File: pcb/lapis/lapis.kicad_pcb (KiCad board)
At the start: 2 copper layers, 42 x 58.6 mm, 80 parts, among them IC1 AS5047P-ATSM, IC2 AS5047P-ATSM, IC3 DRV8835DSSR, IC4 MIC5219-3.3YM5-TR, J1 Conn_01x03, J10 Conn_01x04, J11 Conn_01x01, J12 Conn_01x01, J13 Conn_01x01, J14 Conn_01x01, J2 Conn_01x03, J3 Conn_01x02, J4 Conn_01x03, J5 Conn_01x03, J6 Conn_01x03, J7 Conn_01x03, J8 Conn_01x03, J9 Conn_01x03, Q1 LTR-4206E, Q2 LTR-4206E, Q3 LTR-4206E, Q4 LTR-4206E, Q5 IRLML6402TRPBF, Q6 MMBF0201NLT1G, U1 STM32F411CEUx, U2 ICM-20602, U3 NJU6080, U4 NJU6080

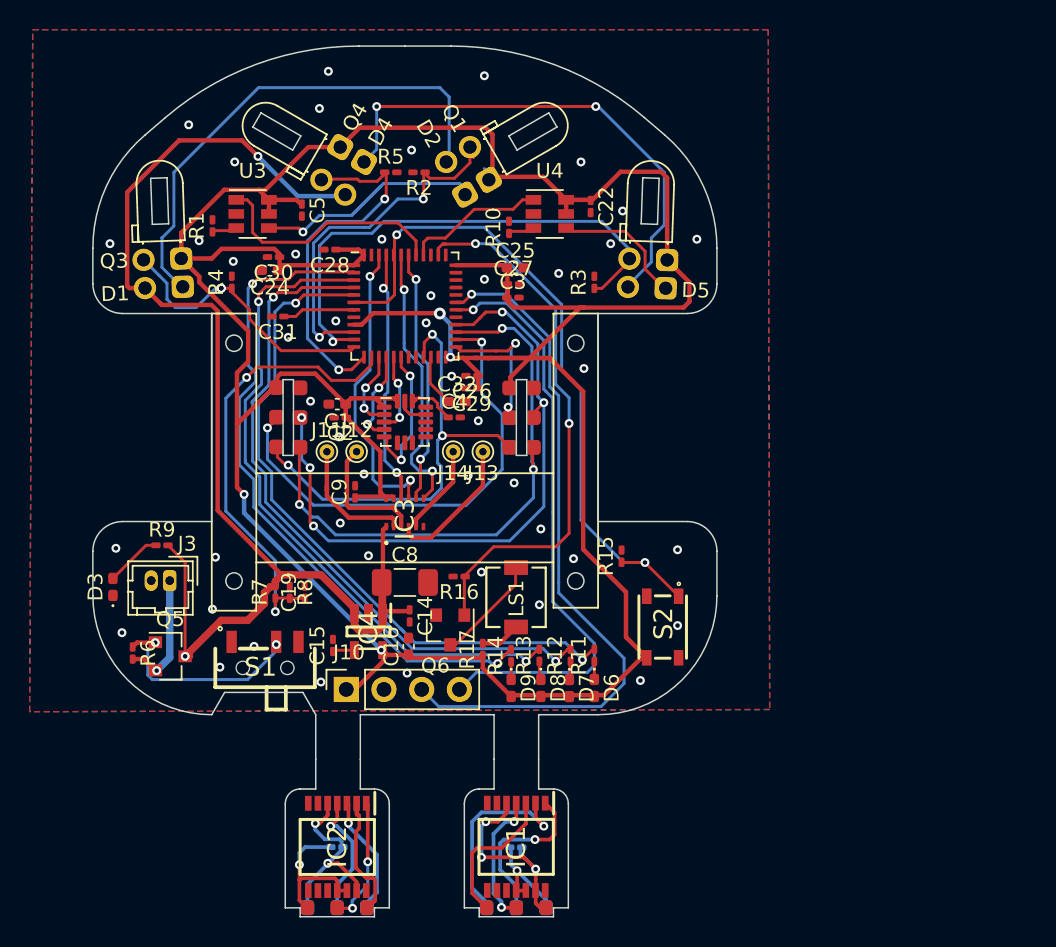
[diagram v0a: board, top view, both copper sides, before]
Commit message: STM411失敗基板　STM484に変更し基板修正
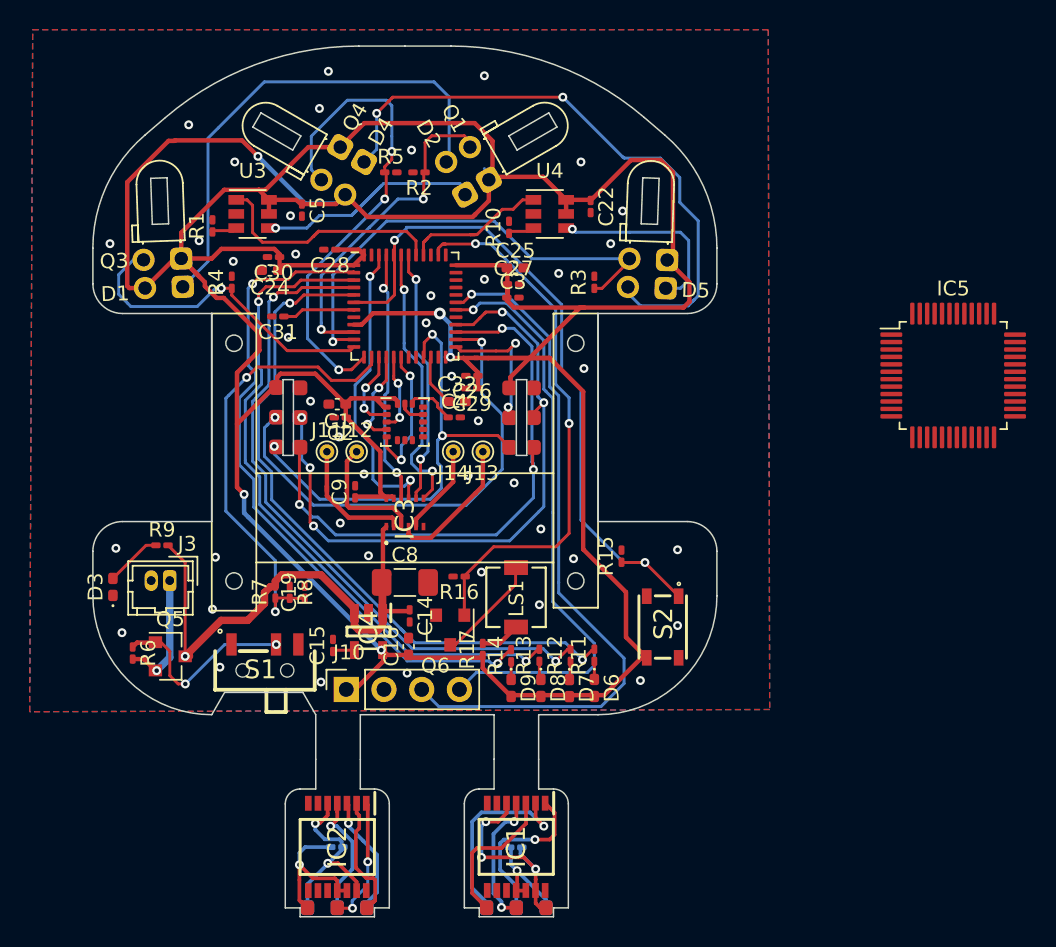
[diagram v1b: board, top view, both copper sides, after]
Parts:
- added IC5: STM32G484CET6, Package_QFP:LQFP-48_7x7mm_P0.5mm, F.Cu at (182.2, 100.9)
- moved S1 0.17 mm to (136.6, 119.0)
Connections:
- D1 pad 2: +BATT -> +3V3
- D4 pad 2: +BATT -> +3V3
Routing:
- net +BATT: track 89.4 -> 39.1 mm, vias 2 -> 1
- net +3V3: track 231.2 -> 279.9 mm, vias 4 -> 5
- net /WALL_SENSOR_LS/WALLSENSOR_ADC: track 25.2 -> 33.6 mm, vias 2 -> 3
- net Net-(D4-Pad1): track 34.0 -> 41.1 mm
- net Net-(D5-Pad1): track 8.41 -> 12.6 mm, vias 0 -> 1
- net /WALL_SENSOR_LF/WALLSENSOR_ADC: track 19.2 -> 22.5 mm, vias 2 -> 1
- net /WALL_SENSOR_RF/WALLSENSOR_ADC: track 34.6 -> 32.4 mm
- net /WALL_SENSOR_RS/WALLSENSOR_ADC: track 25.1 -> 24.0 mm
- net Net-(Q5-Pad1): track 14.0 -> 13.2 mm
- net Net-(D1-Pad1): track 33.9 -> 33.1 mm
- net Net-(C4-Pad1): track 3.78 -> 3.14 mm
- net /CPU/LED_LSRF: track 10.3 -> 10.9 mm
- net GND: vias 46 -> 43

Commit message: no message
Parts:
- removed IC5: STM32G484CET6, Package_QFP:LQFP-48_7x7mm_P0.5mm

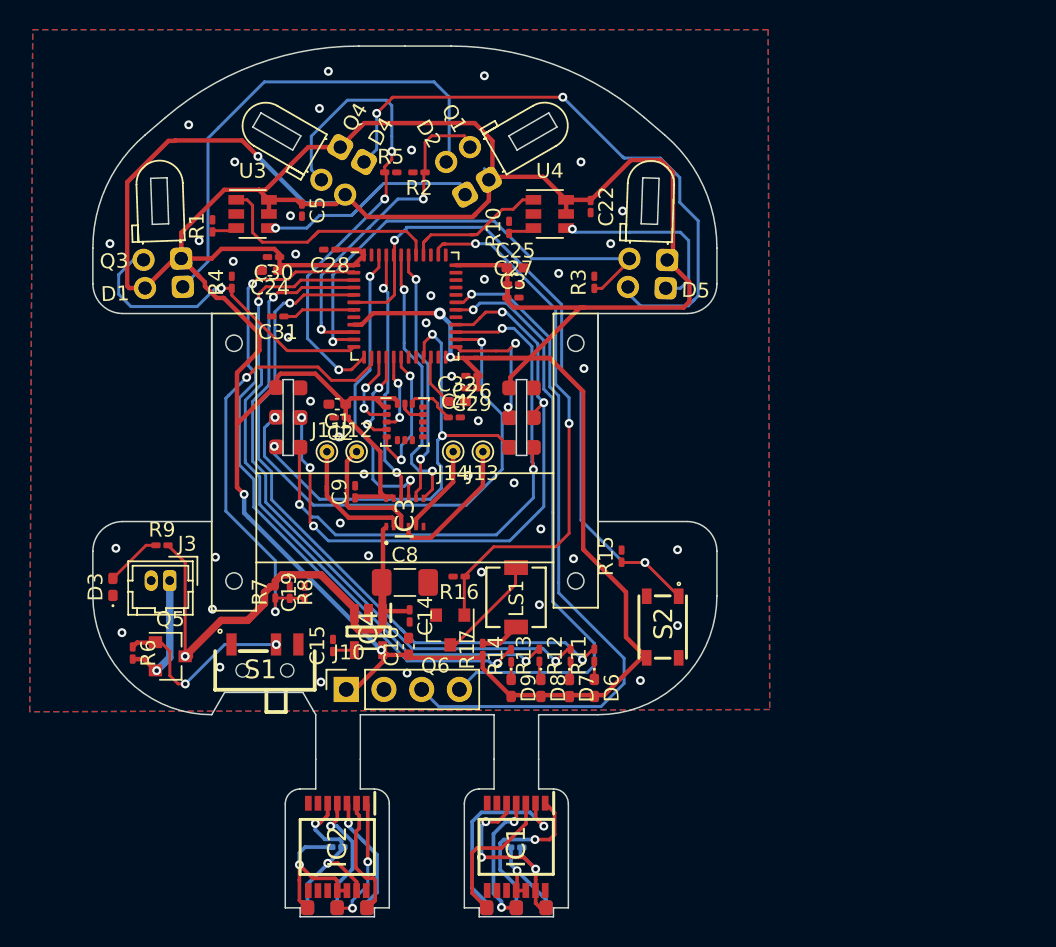
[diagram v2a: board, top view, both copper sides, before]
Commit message: 信地旋回探索
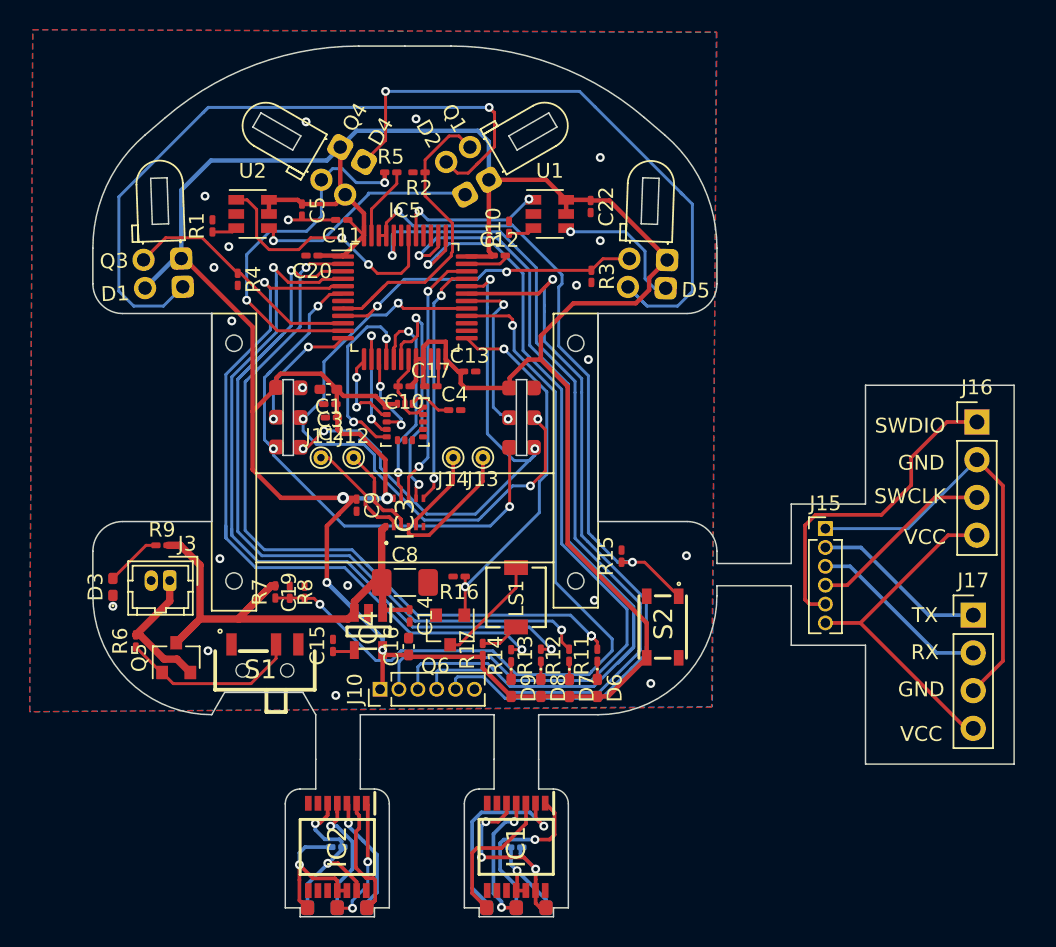
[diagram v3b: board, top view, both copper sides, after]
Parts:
- removed C24, C25, C32: 10u, Capacitor_SMD:C_0402_1005Metric_Pad0.74x0.62mm_HandSolder
- removed C26, C27, C28, C29, C30, C31: 0.1u, Capacitor_SMD:C_0201_0603Metric_Pad0.64x0.40mm_HandSolder
- removed the U1 at (145.2, 96.2)
- added C10: 0.1u, Capacitor_SMD:C_0201_0603Metric_Pad0.64x0.40mm_HandSolder, F.Cu at (145.2, 101.6)
- added C11: 0.1u, Capacitor_SMD:C_0201_0603Metric_Pad0.64x0.40mm_HandSolder, F.Cu at (141.0, 90.4)
- added C12: 0.1u, Capacitor_SMD:C_0201_0603Metric_Pad0.64x0.40mm_HandSolder, F.Cu at (151.6, 92.8)
- added C13: 0.1u, Capacitor_SMD:C_0201_0603Metric_Pad0.64x0.40mm_HandSolder, F.Cu at (149.6, 100.6)
- added C17: 1u, Capacitor_SMD:C_0201_0603Metric_Pad0.64x0.40mm_HandSolder, F.Cu at (147.0, 101.6)
- added C20: 1u, Capacitor_SMD:C_0201_0603Metric_Pad0.64x0.40mm_HandSolder, F.Cu at (139.0, 92.8)
- added IC5: STM32G484CET6, Package_QFP:LQFP-48_7x7mm_P0.5mm, F.Cu at (145.2, 95.6)
- added J15: Conn_01x06_Male, Connector_PinHeader_1.27mm:PinHeader_1x06_P1.27mm_Vertical, F.Cu at (173.6, 111.2)
- added J16: Conn_01x04_Female, Connector_PinHeader_2.54mm:PinHeader_1x04_P2.54mm_Vertical, F.Cu at (183.8, 104.0)
- added J17: Conn_01x04_Female, Connector_PinHeader_2.54mm:PinHeader_1x04_P2.54mm_Vertical, F.Cu at (183.5, 117.0)
- IC1, IC2: footprint SamacSys_Parts:SOP65P640X120-14N -> SOP65P640X120-14N
- IC3: footprint SamacSys_Parts:DRV8835DSSR -> DRV8835DSSR
- IC4: footprint SamacSys_Parts:SOT95P280X130-5N -> SOT95P280X130-5N
- J10: value Conn_01x04 -> Conn_01x06_Female; footprint Connector_PinSocket_2.54mm:PinSocket_1x04_P2.54mm_Vertical -> Connector_PinHeader_1.27mm:PinHeader_1x06_P1.27mm_Vertical
- S1: footprint SamacSys_Parts:SSSS810701 -> SSSS810701
- moved C3 14.3 mm to (140.2, 102.8), turned to 180 degrees
- moved J10 2.28 mm to (143.6, 122.0)
- moved C1 1.17 mm to (140.1, 101.8)
- moved C9 0.91 mm to (142.0, 109.6), turned to 270 degrees
- moved R6 0.84 mm to (127.1, 118.7), turned to 90 degrees
- moved C2 0.60 mm to (140.3, 103.7)
- moved J11 0.57 mm to (139.6, 106.4)
- moved C4 0.49 mm to (148.6, 103.2)
- moved J12 0.45 mm to (141.8, 106.4)
- moved R4 0.45 mm to (134.0, 94.4), turned to 270 degrees
- moved R3 0.45 mm to (157.8, 94.2), turned to 270 degrees
- moved Q5 0.41 mm to (129.9, 119.9), turned to 90 degrees
- moved J13 0.40 mm to (150.5, 106.4)
- moved J14 0.40 mm to (148.5, 106.4)
- moved D6 0.20 mm to (158.2, 121.9)
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- renumbered U4 to U1, U3 to U2, U2 to U3
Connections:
- net /CPU/SPEAKER renamed /CPU/BUZZER
- IC3 pad 10: /CPU/ML_PWM -> /CPU/ML_PHASE
- IC3 pad 8: /CPU/MR_PWM -> /CPU/MR_PHASE
- J10 pad 2: GND -> /CPU/SWDIO
- J10 pad 3: /CPU/RX -> /CPU/SWCLK
- J10 pad 4: /CPU/TX -> /CPU/RX
- R11 pad 2: /CPU/LED0 -> /UI/LED1
- R12 pad 2: /CPU/LED1 -> /UI/LED2
- R13 pad 2: /CPU/LED2 -> /UI/LED3
- R14 pad 2: /CPU/LED3 -> /UI/LED4
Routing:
- net +3V3: track 279.9 -> 212.2 mm, vias 5 -> 4
- net /CPU/SWCLK: track 0.00 -> 63.3 mm, vias 0 -> 1
- net /CPU/SWDIO: track 0.00 -> 57.4 mm, vias 0 -> 1
- net /UI/LED2: track 0.00 -> 54.0 mm, vias 0 -> 2
- net /UI/LED1: track 0.00 -> 52.2 mm, vias 0 -> 3
- net /UI/LED3: track 0.00 -> 52.2 mm, vias 0 -> 2
- net /UI/LED4: track 0.00 -> 48.7 mm, vias 0 -> 2
- net /CPU/LED0: track 46.3 -> 0.00 mm, vias 2 -> 0
- net /CPU/LED2: track 45.8 -> 0.00 mm, vias 2 -> 0
- net /CPU/LED1: track 45.8 -> 0.00 mm, vias 2 -> 0
- net /CPU/LED3: track 45.6 -> 0.00 mm, vias 2 -> 0
- net GND: track 2.24 -> 47.5 mm, vias 43 -> 20
- net /POWER/AD_BATT: track 30.6 -> 54.6 mm
- net /MOTOR_ENCODER_L/ENC_CS: track 32.4 -> 8.69 mm
- net VCC: track 0.00 -> 22.7 mm
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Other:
- board size 42 x 58.6 mm -> 62 x 58.6 mm
- board text added: "RX"
- board text added: "SWCLK"
- board text added: "SWDIO"
- board text added: "SWIO"
- board text added: "TX"
- board text added: "VCC"
- board text added: "lapis COM Board v1.0"
- board text added: "lapis v3.0"
- board text removed: "RXD"
- board text removed: "TXD"
- board text removed: "lapis v2.0"

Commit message: PC切り替え　Kicadv6に変更
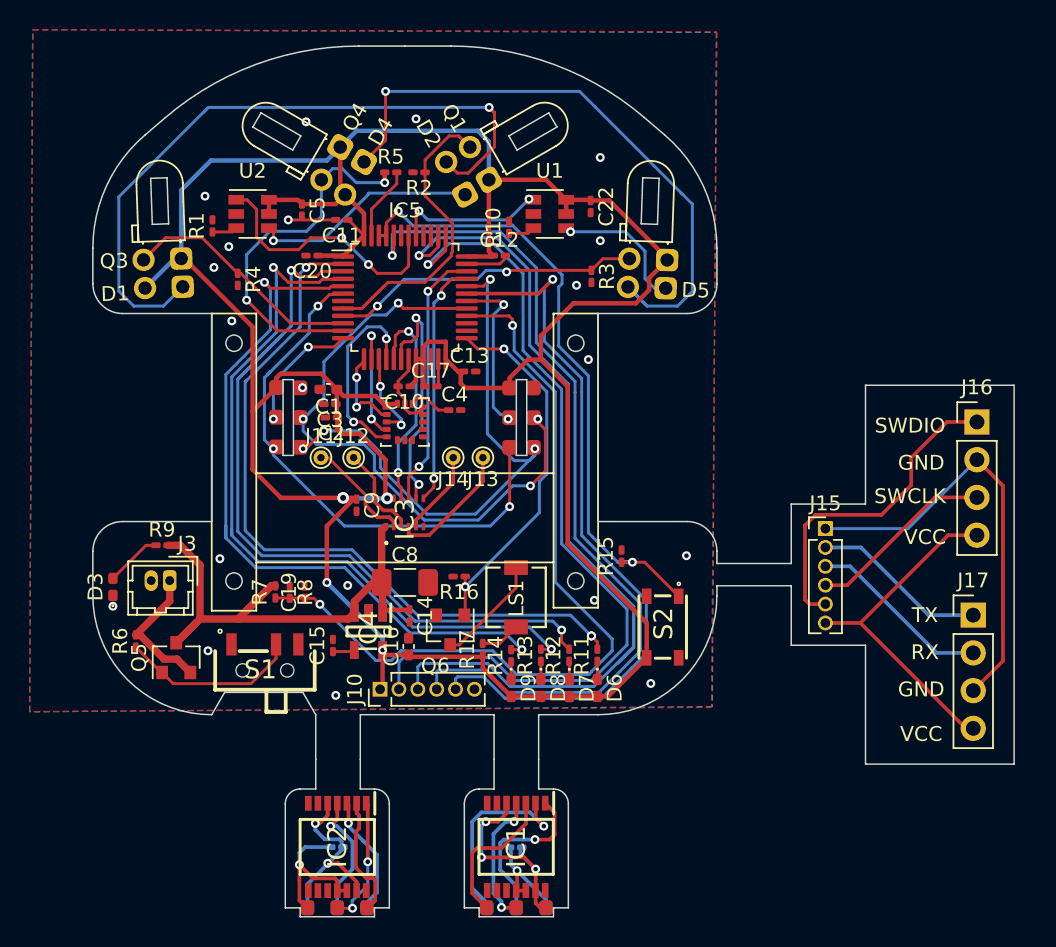
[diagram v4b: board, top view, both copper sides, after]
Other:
- outline, holes or cut-outs redrawn
- net class BATT removed
- net class Default removed
- net class POWER removed
